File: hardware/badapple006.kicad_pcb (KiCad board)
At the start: 2 copper layers, 16.4 x 16.2 mm, 35 parts, among them J1 OLED, J10 SCL, J11 SDA, J2 USB_C_Receptacle_USB2.0, J3 PG, J4 3.3, J5 GND, J6 RFO, J7 RFA, J8 APPLE, J9 RFO2, U1 CH32V006F8U6, U2 RS3236-3.3YUTDN4, Y1 24MHz

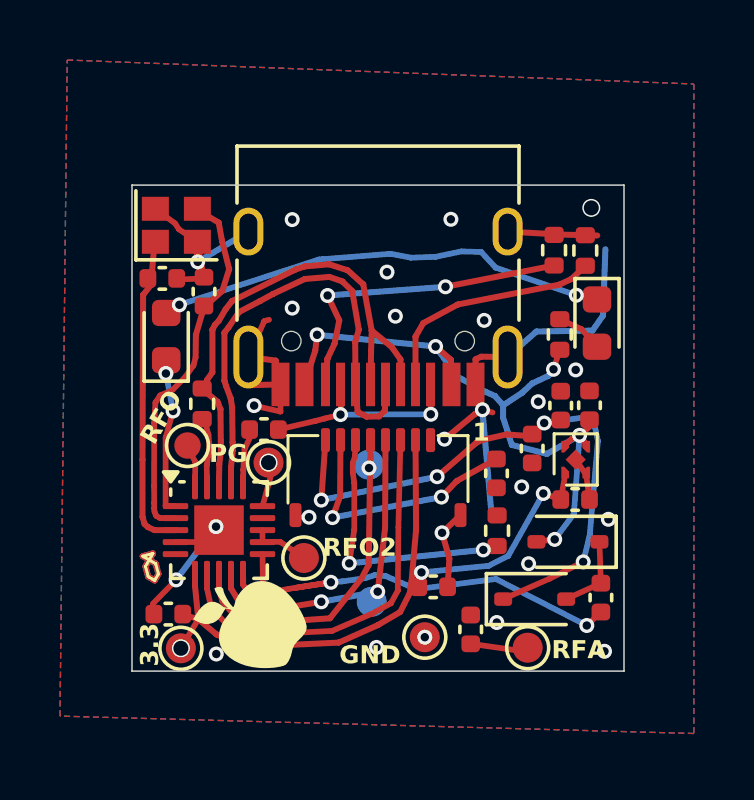
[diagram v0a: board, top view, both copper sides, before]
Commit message: Update design for new Ronbo OLED
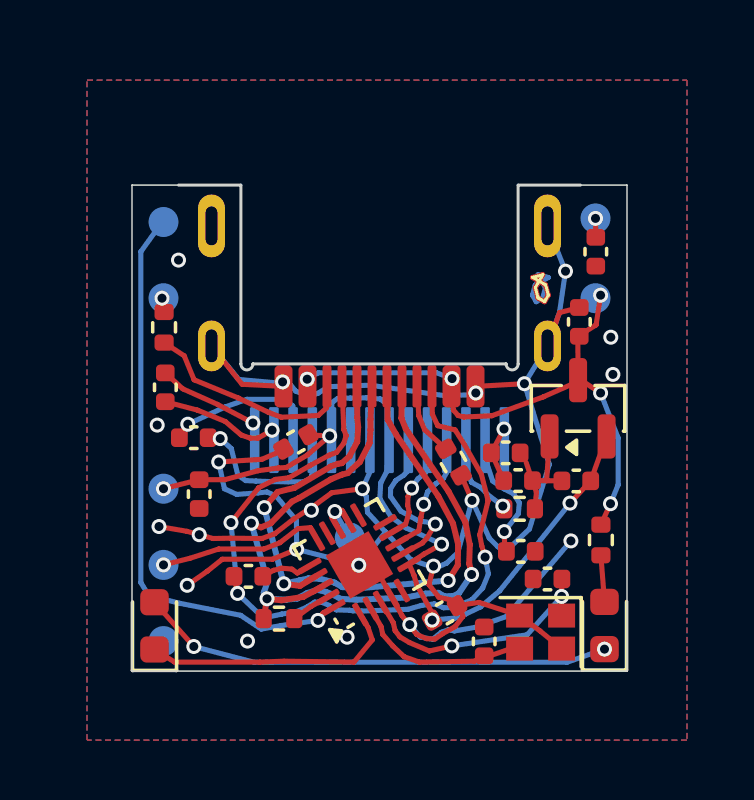
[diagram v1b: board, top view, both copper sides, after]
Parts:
- removed C1, C2, C5: 4.7u10v, Capacitor_SMD:C_0402_1005Metric
- removed C3: 100n, Capacitor_SMD:C_0402_1005Metric
- removed D3, D4: D, Diode_SMD:D_SOD-323
- removed J1: OLED, fpc:AFC42-S08FMA-1H
- added C13: 1u, Capacitor_SMD:C_0402_1005Metric, F.Cu at (71.1, 86.7)
- added C14: 1u, Capacitor_SMD:C_0402_1005Metric, F.Cu at (72.1, 88.4)
- added C15: 1u, Capacitor_SMD:C_0402_1005Metric, F.Cu at (72.2, 90.3)
- added C16: 1u, Capacitor_SMD:C_0402_1005Metric, F.Cu at (80.4, 94.3)
- added C17: 4.7u10v, Capacitor_SMD:C_0402_1005Metric, F.Cu at (82.9, 89.8)
- added C18: 100n, Capacitor_SMD:C_0402_1005Metric, F.Cu at (82.5, 88.9)
- added J12: RB066-6448-TSWHG01, cnhardware:OLED-RB066-6448TSWHG01, B.Cu at (78.2, 88.5)
- C12: value 4.7u10v -> 10u6.3v
- J10: value SCL -> 5V
- J11: value SDA -> GND
- J2: footprint Connector_USB:USB_C_Receptacle_HRO_TYPE-C-31-M-12 -> cnhardware:USB_C_TIGHT_IN_BOARD_161N-4BC21665
- J3, J5, J6, J7, J8, J9: moved to B.Cu
- J4: value 3.3 -> 3v3; moved to B.Cu
- U2: value RS3236-3.3YUTDN4 -> XC6206P332; footprint cnhardware:xdfn-reg -> Package_TO_SOT_SMD:SOT-23
- moved Y1 18.2 mm to (83.6, 94.9), turned to 180 degrees
- moved C9 16.3 mm to (83.8, 93.1), turned to 0 degrees
- moved C10 14.9 mm to (81.7, 95.2)
- moved J7 14.5 mm to (85.5, 81.1), turned to 180 degrees
- moved C8 13.3 mm to (85.5, 82.2), turned to -90 degrees
- moved R3 13.3 mm to (71.1, 84.7)
- moved J10 12.6 mm to (85.5, 83.8)
- moved J8 10.6 mm to (84.6, 94.1), turned to 150 degrees
- moved D2 10.1 mm to (85.8, 94.7), turned to 90 degrees
- moved D1 9.65 mm to (70.8, 94.7)
- moved J11 8.82 mm to (71.0, 83.8)
- moved J5 8.71 mm to (71.0, 95.2), turned to 180 degrees
- moved R2 8.31 mm to (80.7, 89.2), turned to -60 degrees
- moved R4 7.60 mm to (74.9, 94.5), turned to 180 degrees
- moved J6 7.49 mm to (71.0, 81.2), turned to 180 degrees
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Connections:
- C11 pad 2: CHARGEPUMP -> GND
- J10 pad 1: SCL -> VBUS
- J11 pad 1: SDA -> GND
- U1 pad 10: CHARGEPUMP -> CHARGEPUMPB
- U2 pad 1: OVDD -> GND
- U2 pad 2: GND -> OVDD
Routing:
- net GND: track 40.7 -> 83.9 mm, vias 25 -> 23
- net OVCC: track 20.1 -> 0.00 mm, vias 4 -> 0
- net Net-(J2-SBU1): track 7.63 -> 26.1 mm, vias 2 -> 3
- net RFO: track 1.31 -> 19.4 mm, vias 0 -> 1
- net CHARGEPUMP: track 16.1 -> 0.00 mm, vias 2 -> 0
- net D-: track 16.9 -> 26.5 mm, vias 0 -> 3
- net Net-(J1-Pin_2): track 8.58 -> 0.00 mm, vias 2 -> 0
- net RES: track 13.4 -> 5.60 mm, vias 0 -> 1
- net SCL: track 11.0 -> 3.69 mm, vias 2 -> 1
- net SDA: track 11.5 -> 4.25 mm
- net Net-(U1-PA1/T1/T2/OPN0/XI/A1): track 12.3 -> 5.65 mm
- net D+: track 16.0 -> 22.4 mm, vias 0 -> 3
- net Net-(J12-Pin_12): track 9.10 -> 2.85 mm, vias 2 -> 1
- net Net-(J12-Pin_4): track 0.00 -> 5.69 mm, vias 0 -> 1
- net Net-(J2-CC1): track 7.95 -> 2.44 mm
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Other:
- board size 16.4 x 16.2 mm -> 16.5 x 16.2 mm
- board text added: "badderapple"
- board text removed: "1"
- board text removed: "badapple006 flip rev B(ad)"

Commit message: Update to what was really orderedo
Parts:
- C11, C17, C4, C6: footprint Capacitor_SMD:C_0402_1005Metric -> Capacitor_SMD:C_0603_1608Metric
- U1: value CH32V006F8U6 -> CH32V006F8U7
- U2: value XC6206P332 -> XC6206P362
- moved C15 13.7 mm to (86.0, 90.4)
- moved C4 13.1 mm to (71.8, 90.8), turned to -90 degrees
- moved R1 2.19 mm to (82.2, 88.7)
- moved C7 1.65 mm to (74.0, 89.3), turned to 180 degrees
- moved C9 1.46 mm to (85.0, 92.3), turned to -90 degrees
- moved C17 1.07 mm to (83.3, 90.8)
- moved C6 0.81 mm to (85.5, 84.0)
- moved C18 0.77 mm to (82.7, 89.7)
- moved C8 0.75 mm to (85.4, 81.5), turned to 180 degrees
- moved R5 0.57 mm to (86.0, 92.3)
- moved C12 0.31 mm to (73.9, 93.3)
- moved J12 0.30 mm to (78.2, 88.8)
- moved J2 0.30 mm to (78.2, 81.7)
- moved R2 0.27 mm to (80.7, 89.5), turned to -57 degrees
- moved C11 0.15 mm to (83.1, 92.3)
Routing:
- net GND: track 83.9 -> 77.1 mm, vias 23 -> 25
- net Net-(J12-Pin_14): track 1.91 -> 4.81 mm
- net Net-(J12-Pin_12): track 2.85 -> 0.92 mm
- net Net-(J12-Pin_13): track 4.21 -> 5.72 mm
- net RES: track 5.60 -> 6.40 mm
- net Net-(J12-Pin_2): track 3.95 -> 4.59 mm
- net Net-(U1-PA2/T1/T2/U2TX_/OPP0/X0A0): track 8.65 -> 9.26 mm
- net SCL: track 3.69 -> 3.14 mm
- net Net-(J12-Pin_4): track 5.69 -> 6.20 mm

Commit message: Update to new ch32fun, working build.
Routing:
- net SCL: track 3.14 -> 3.89 mm
- net VBUS: track 19.4 -> 18.9 mm, vias 5 -> 6

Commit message: Update hardware
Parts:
- moved J7 14.5 mm to (71.0, 83.1)
- moved C8 14.5 mm to (71.0, 83.0)
- moved J6 12.0 mm to (71.0, 93.2)
- moved J11 2.69 mm to (71.1, 81.1)
- moved J10 2.67 mm to (85.4, 81.1)
- moved J3 1.46 mm to (71.0, 91.2)
- moved J4 0.92 mm to (71.0, 89.2)
- moved J12 0.10 mm to (78.2, 88.9)
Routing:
- net GND: track 77.1 -> 93.6 mm, vias 25 -> 23
- net RFO: track 19.5 -> 6.56 mm
- net VBUS: track 18.9 -> 21.6 mm
- net SWIO: track 5.66 -> 6.78 mm
- net OVDD: track 28.3 -> 27.2 mm
- net Net-(J12-Pin_13): track 5.72 -> 5.01 mm
- net D-: track 26.5 -> 27.0 mm

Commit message: * Move to rev B, bigger connectors, fix some messed up connections.  * Make `make all` make everything.
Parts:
- moved J9 0.71 mm to (76.6, 92.0)
- moved J11 0.11 mm to (71.1, 81.2)
- moved J7 0.11 mm to (71.0, 83.2)
- moved J10 0.10 mm to (85.4, 81.2)
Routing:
- net GND: track 93.6 -> 93.0 mm, vias 23 -> 26
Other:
- board text added: "+"
- board text added: "+5v"
- board text added: "-"
- board text added: "RB066-6448TWHG01"
- board text added: "rev b"

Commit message: Update hardware
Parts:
- moved C18 2.46 mm to (85.1, 90.4), turned to -90 degrees
- moved C10 2.41 mm to (84.1, 95.6), turned to 180 degrees
- moved C11 1.51 mm to (82.4, 91.0), turned to -90 degrees
- moved Y1 1.13 mm to (83.2, 93.9)
- moved C17 0.64 mm to (83.8, 91.1), turned to -90 degrees
- moved C16 0.47 mm to (80.7, 93.9)
- moved J9 0.35 mm to (76.6, 92.4)
- moved R2 0.27 mm to (80.5, 89.4), turned to -50 degrees
- moved C14 0.27 mm to (71.8, 88.5)
- moved J2 0.16 mm to (78.2, 81.8)
- moved C13 0.15 mm to (71.0, 86.6)
- moved R1 0.11 mm to (82.2, 88.6)
- moved J12 0.10 mm to (78.2, 89.0)
- moved C9 0.06 mm to (85.0, 92.2)
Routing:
- net GND: track 93.0 -> 105.3 mm, vias 26 -> 25
- net Net-(J12-Pin_13): track 5.01 -> 7.61 mm
- net Net-(U1-PA1/T1/T2/OPN0/XI/A1): track 5.65 -> 7.12 mm
- net REDCOLOR: track 8.67 -> 7.90 mm
- net D-: track 27.0 -> 27.6 mm
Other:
- outline, holes or cut-outs redrawn
- board text added: "* Red 1.2mm thick * OSP or ENIG * 5x5 with side rails"
- board text added: "rev bad"
- board text removed: "rev b"
